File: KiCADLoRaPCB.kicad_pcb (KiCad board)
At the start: 2 copper layers, 114.8 x 80 mm, 13 parts, among them J1 Raspberry_Pi_2_3, J2 RHF-GW, J3 Jack-DC

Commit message: edge cut layer of the square case cut are refined mistakes
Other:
- board size 114.8 x 80 mm -> 114.8 x 85.1 mm
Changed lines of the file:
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@@
     (links 33)
     (no_connects 33)
-    (area 60.884999 48.184999 175.843001 128.345001)
+    (area 60.884999 47.925 175.843001 142.600001)
     (thickness 1.6)
-    (drawings 2924)
+    (drawings 2933)
     (tracks 0)
     (zones 0)
@@
     (pad 1 np_thru_hole circle (at 0 0) (size 4.3 4.3) (drill 4.3) (layers *.Cu *.Mask))
   )
-  (gr_line (start 175.768 128.27) (end 151.13 128.27) (angle 90) (layer Edge.Cuts) (width 0.15))
+  (gr_line (start 60.96 48.26) (end 60.96 55.88) (angle 90) (layer Edge.Cuts) (width 0.15))
+  (gr_line (start 60.96 58.42) (end 60.96 60.96) (angle 90) (layer Edge.Cuts) (width 0.15))
+  (gr_line (start 60.96 115.57) (end 60.96 118.11) (angle 90) (layer Edge.Cuts) (width 0.15))
+  (gr_line (start 60.96 128.27) (end 60.96 120.65) (angle 90) (layer Edge.Cuts) (width 0.15))
+  (gr_line (start 175.768 45.72) (end 175.768 48.26) (angle 90) (layer Edge.Cuts) (width 0.15))
+  (gr_line (start 60.96 45.72) (end 175.768 45.72) (angle 90) (layer Edge.Cuts) (width 0.15))
+  (gr_line (start 60.96 48.26) (end 60.96 45.72) (angle 90) (layer Edge.Cuts) (width 0.15))
+  (gr_line (start 60.96 130.81) (end 60.96 128.27) (angle 90) (layer Edge.Cuts) (width 0.15))
+  (gr_line (start 175.768 130.81) (end 175.768 128.27) (angle 90) (layer Edge.Cuts) (width 0.15))
+  (gr_line (start 60.96 130.81) (end 175.768 130.81) (angle 90) (layer Edge.Cuts) (width 0.15))
+  (gr_line (start 65.024 58.42) (end 64.77 58.42) (angle 90) (layer Edge.Cuts) (width 0.15))
+  (gr_line (start 65.024 55.88) (end 65.024 58.42) (angle 90) (layer Edge.Cuts) (width 0.15))
+  (gr_line (start 64.77 55.88) (end 65.024 55.88) (angle 90) (layer Edge.Cuts) (width 0.15))
+  (gr_line (start 65.024 120.65) (end 64.77 120.65) (angle 90) (layer Edge.Cuts) (width 0.15))
+  (gr_line (start 65.024 118.11) (end 65.024 120.65) (angle 90) (layer Edge.Cuts) (width 0.15))
+  (gr_line (start 64.77 118.11) (end 65.024 118.11) (angle 90) (layer Edge.Cuts) (width 0.15))
+  (gr_line (start 60.96 115.57) (end 60.96 114.3) (angle 90) (layer Edge.Cuts) (width 0.15))
+  (gr_line (start 64.77 118.11) (end 60.96 118.11) (angle 90) (layer Edge.Cuts) (width 0.15))
+  (gr_line (start 60.96 120.65) (end 64.77 120.65) (angle 90) (layer Edge.Cuts) (width 0.15))
   (gr_line (start 175.768 48.26) (end 175.768 128.27) (angle 90) (layer Edge.Cuts) (width 0.15))
-  (gr_line (start 151.13 48.26) (end 175.768 48.26) (angle 90) (layer Edge.Cuts) (width 0.15))
   (gr_line (start 169 59.5) (end 169 142.5) (angle 90) (layer Dwgs.User) (width 0.2))
   (gr_line (start 169 142.5) (end 169.5 142.5) (angle 90) (layer Dwgs.User) (width 0.2))
@@
   (gr_line (start 72.39 59.69) (end 115.316 59.69) (angle 90) (layer Dwgs.User) (width 0.2))
   (gr_line (start 67.818 59.69) (end 72.39 59.69) (angle 90) (layer Dwgs.User) (width 0.2))
-  (gr_line (start 67.818 59.69) (end 64.77 59.69) (angle 90) (layer Eco1.User) (width 0.2))
-  (gr_line (start 60.96 118.11) (end 60.96 128.27) (angle 90) (layer Edge.Cuts) (width 0.15))
+  (gr_line (start 67.818 57.15) (end 64.77 57.15) (angle 90) (layer Eco1.User) (width 0.2))
   (gr_line (start 60.96 60.96) (end 60.96 114.3) (angle 90) (layer Edge.Cuts) (width 0.15))
-  (gr_line (start 64.77 114.3) (end 60.96 114.3) (angle 90) (layer Edge.Cuts) (width 0.15))
-  (gr_line (start 64.77 118.11) (end 64.77 114.3) (angle 90) (layer Edge.Cuts) (width 0.15))
-  (gr_line (start 60.96 118.11) (end 64.77 118.11) (angle 90) (layer Edge.Cuts) (width 0.15))
-  (gr_line (start 60.96 48.26) (end 60.96 58.42) (angle 90) (layer Edge.Cuts) (width 0.15))
-  (gr_line (start 64.77 60.96) (end 60.96 60.96) (angle 90) (layer Edge.Cuts) (width 0.15))
-  (gr_line (start 64.77 58.42) (end 64.77 60.96) (angle 90) (layer Edge.Cuts) (width 0.15))
-  (gr_line (start 60.96 58.42) (end 64.77 58.42) (angle 90) (layer Edge.Cuts) (width 0.15))
-  (gr_line (start 151.13 48.26) (end 60.96 48.26) (angle 90) (layer Edge.Cuts) (width 0.15))
-  (gr_line (start 60.96 128.27) (end 151.13 128.27) (angle 90) (layer Edge.Cuts) (width 0.15))
+  (gr_line (start 64.77 58.42) (end 60.96 58.42) (angle 90) (layer Edge.Cuts) (width 0.15))
+  (gr_line (start 60.96 55.88) (end 64.77 55.88) (angle 90) (layer Edge.Cuts) (width 0.15))
 )

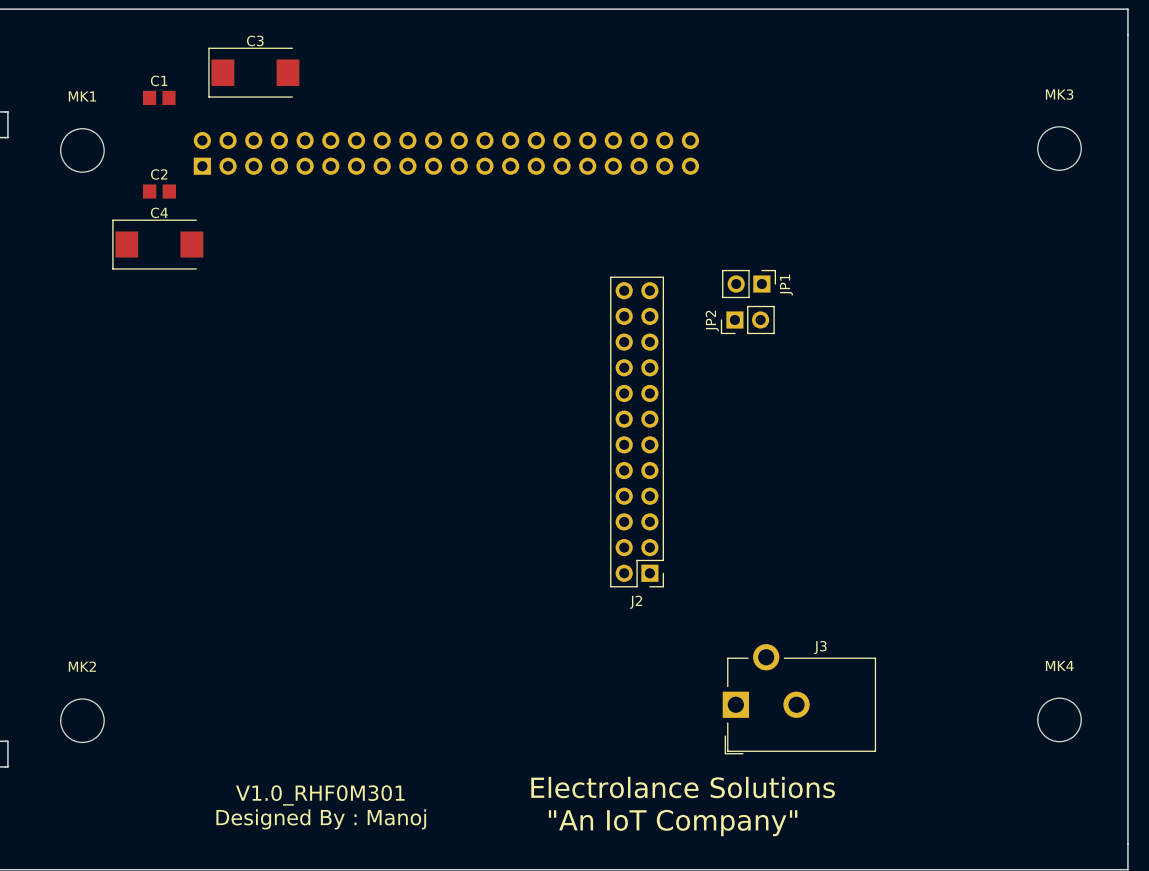
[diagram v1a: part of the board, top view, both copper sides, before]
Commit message: All holes ext PCB alignedwith case hole
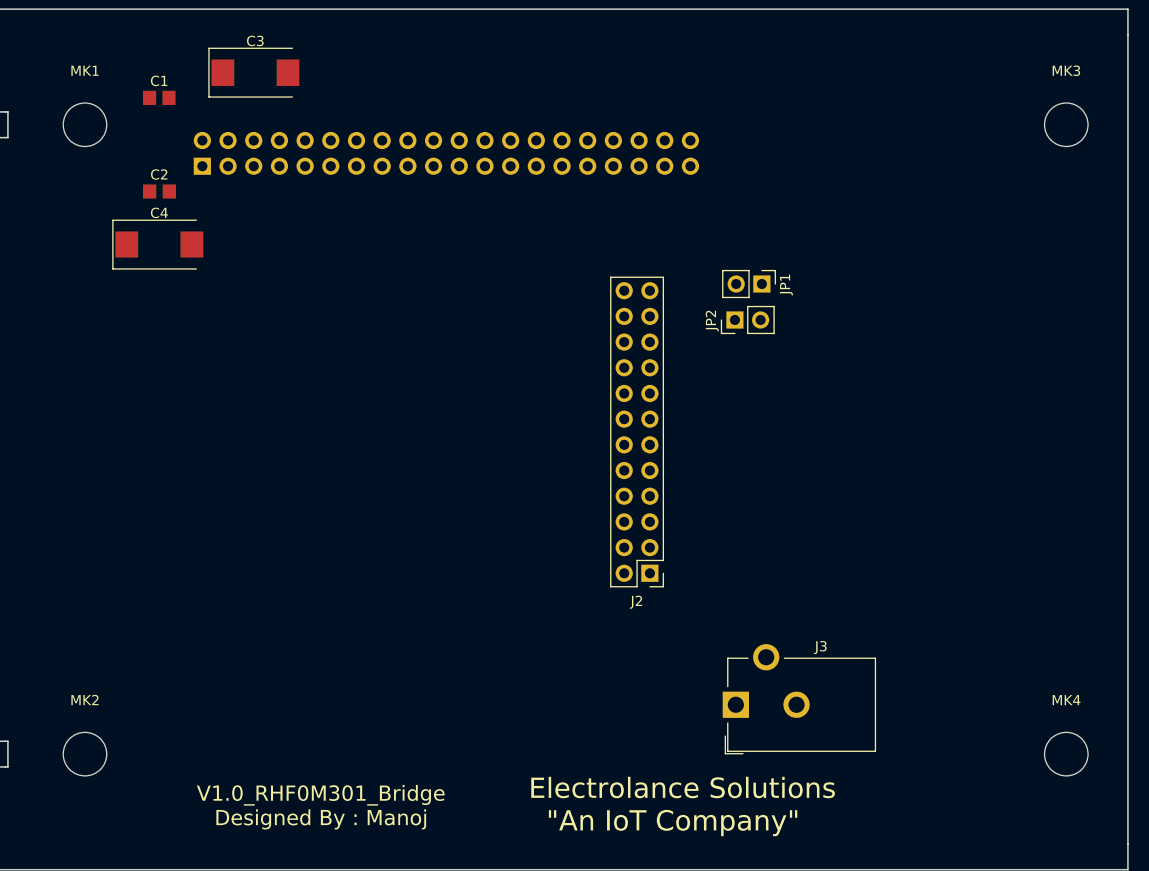
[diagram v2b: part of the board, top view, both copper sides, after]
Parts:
- moved MK4 3.45 mm to (169.7, 119.4)
- moved MK2 3.31 mm to (72.6, 119.4)
- moved MK1 2.55 mm to (72.6, 57.1)
- moved MK3 2.44 mm to (169.7, 57.1)
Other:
- board text added: "8.5 x 11.5 [cm]"
- board text added: "Edge cut till border S. Hole"
- board text added: "V1.0_RHF0M301_Bridge Designed By : Manoj"
- board text removed: "V1.0_RHF0M301 Designed By : Manoj"
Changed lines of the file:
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@@
     (links 33)
     (no_connects 33)
-    (area 60.884999 47.925 175.843001 142.600001)
+    (area 60.884999 45.644999 175.843001 130.885001)
     (thickness 1.6)
-    (drawings 2933)
+    (drawings 2956)
     (tracks 0)
     (zones 0)
@@
     (visible_elements FFFFF77F)
     (pcbplotparams
-      (layerselection 0x00030_80000001)
+      (layerselection 0x01000_00000000)
       (usegerberextensions false)
       (excludeedgelayer true)
@@
       (padsonsilk false)
       (subtractmaskfromsilk false)
-      (outputformat 1)
+      (outputformat 4)
       (mirror false)
-      (drillshape 1)
+      (drillshape 0)
       (scaleselection 1)
-      (outputdirectory ""))
+      (outputdirectory Gerber&Schematics/))
   )
   (net 0 "")
@@
   )
   (module MountingHole:MountingHole_4.3mm_M4 (layer F.Cu)
-    (at 72.39 59.69)
+    (at 72.644 57.15)
     (descr "Mounting Hole 4.3mm, no annular, M4")
     (tags "mounting hole 4.3mm no annular m4")
@@
   )
   (module MountingHole:MountingHole_4.3mm_M4 (layer F.Cu)
-    (at 72.39 116.078)
+    (at 72.644 119.38)
     (descr "Mounting Hole 4.3mm, no annular, M4")
     (tags "mounting hole 4.3mm no annular m4")
@@
   )
   (module MountingHole:MountingHole_4.3mm_M4 (layer F.Cu)
-    (at 169 59.5)
+    (at 169.672 57.15)
     (descr "Mounting Hole 4.3mm, no annular, M4")
     (tags "mounting hole 4.3mm no annular m4")
@@
   )
   (module MountingHole:MountingHole_4.3mm_M4 (layer F.Cu)
-    (at 169 116)
+    (at 169.672 119.38)
     (descr "Mounting Hole 4.3mm, no annular, M4")
     (tags "mounting hole 4.3mm no annular m4")
@@
     (pad 1 np_thru_hole circle (at 0 0) (size 4.3 4.3) (drill 4.3) (layers *.Cu *.Mask))
   )
+  (gr_line (start 67.564 119.38) (end 67.818 119.38) (angle 90) (layer Eco2.User) (width 0.2))
+  (gr_line (start 67.056 119.38) (end 67.31 119.38) (angle 90) (layer Eco2.User) (width 0.2))
+  (gr_line (start 66.548 119.38) (end 66.802 119.38) (angle 90) (layer Eco2.User) (width 0.2))
+  (gr_line (start 66.04 119.38) (end 66.294 119.38) (angle 90) (layer Eco2.User) (width 0.2))
+  (gr_line (start 65.532 119.38) (end 65.786 119.38) (angle 90) (layer Eco2.User) (width 0.2))
+  (gr_line (start 65.024 119.38) (end 65.278 119.38) (angle 90) (layer Eco2.User) (width 0.2))
+  (dimension 7.62 (width 0.3) (layer Margin)
+    (gr_text "7.620 mm" (at 69.596 37.084) (layer Margin)
+      (effects (font (size 1.5 1.5) (thickness 0.3)))
+    )
+    (feature1 (pts (xy 72.644 57.15) (xy 72.644 37.686)))
+    (feature2 (pts (xy 65.024 57.15) (xy 65.024 37.686)))
+    (crossbar (pts (xy 65.024 40.386) (xy 72.644 40.386)))
+    (arrow1a (pts (xy 72.644 40.386) (xy 71.517496 40.972421)))
+    (arrow1b (pts (xy 72.644 40.386) (xy 71.517496 39.799579)))
+    (arrow2a (pts (xy 65.024 40.386) (xy 66.150504 40.972421)))
+    (arrow2b (pts (xy 65.024 40.386) (xy 66.150504 39.799579)))
+  )
+  (dimension 4.064 (width 0.1) (layer Margin)
+    (gr_text "4.064 mm" (at 63.246 138.43) (layer Margin)
+      (effects (font (size 1 1) (thickness 0.1)))
+    )
+    (feature1 (pts (xy 65.024 120.65) (xy 65.024 137.32)))
+    (feature2 (pts (xy 60.96 120.65) (xy 60.96 137.32)))
+    (crossbar (pts (xy 60.96 134.62) (xy 65.024 134.62)))
+    (arrow1a (pts (xy 65.024 134.62) (xy 63.897496 135.206421)))
+    (arrow1b (pts (xy 65.024 134.62) (xy 63.897496 134.033579)))
+    (arrow2a (pts (xy 60.96 134.62) (xy 62.086504 135.206421)))
+    (arrow2b (pts (xy 60.96 134.62) (xy 62.086504 134.033579)))
+  )
+  (gr_text "Edge cut\ntill border\nS. Hole\n" (at 67.056 44.45) (layer Margin)
+    (effects (font (size 0.5 0.5) (thickness 0.1)))
+  )
+  (gr_line (start 79.756 57.15) (end 80.264 57.15) (angle 90) (layer Eco2.User) (width 0.2))
+  (gr_line (start 78.74 57.15) (end 79.248 57.15) (angle 90) (layer Eco2.User) (width 0.2))
+  (gr_line (start 77.724 57.15) (end 78.232 57.15) (angle 90) (layer Eco2.User) (width 0.2))
+  (gr_line (start 76.708 57.15) (end 77.216 57.15) (angle 90) (layer Eco2.User) (width 0.2))
+  (gr_line (start 75.946 57.15) (end 76.454 57.15) (angle 90) (layer Eco2.User) (width 0.2))
+  (gr_line (start 74.93 57.15) (end 75.438 57.15) (angle 90) (layer Eco2.User) (width 0.2))
+  (gr_line (start 69.342 57.15) (end 69.85 57.15) (angle 90) (layer Eco2.User) (width 0.2))
+  (gr_line (start 68.326 57.15) (end 68.834 57.15) (angle 90) (layer Eco2.User) (width 0.2))
+  (gr_line (start 67.31 57.15) (end 67.818 57.15) (angle 90) (layer Eco2.User) (width 0.2))
+  (gr_line (start 66.294 57.15) (end 66.802 57.15) (angle 90) (layer Eco2.User) (width 0.2))
+  (gr_line (start 65.024 57.15) (end 65.786 57.15) (angle 90) (layer Eco2.User) (width 0.2))
+  (dimension 3.048 (width 0.15) (layer Margin)
+    (gr_text "3.048 mm" (at 68.326 46.736) (layer Margin)
+      (effects (font (size 0.8 0.8) (thickness 0.15)))
+    )
+    (feature1 (pts (xy 68.072 57.15) (xy 68.072 47.338)))
+    (feature2 (pts (xy 65.024 57.15) (xy 65.024 47.338)))
+    (crossbar (pts (xy 65.024 50.038) (xy 68.072 50.038)))
+    (arrow1a (pts (xy 68.072 50.038) (xy 66.945496 50.624421)))
+    (arrow1b (pts (xy 68.072 50.038) (xy 66.945496 49.451579)))
+    (arrow2a (pts (xy 65.024 50.038) (xy 66.150504 50.624421)))
+    (arrow2b (pts (xy 65.024 50.038) (xy 66.150504 49.451579)))
+  )
+  (dimension 114.808 (width 0.3) (layer Margin)
+    (gr_text "114.808 mm" (at 118.364 33.956) (layer Margin)
+      (effects (font (size 1.5 1.5) (thickness 0.3)))
+    )
+    (feature1 (pts (xy 175.768 45.72) (xy 175.768 32.606)))
+    (feature2 (pts (xy 60.96 45.72) (xy 60.96 32.606)))
+    (crossbar (pts (xy 60.96 35.306) (xy 175.768 35.306)))
+    (arrow1a (pts (xy 175.768 35.306) (xy 174.641496 35.892421)))
+    (arrow1b (pts (xy 175.768 35.306) (xy 174.641496 34.719579)))
+    (arrow2a (pts (xy 60.96 35.306) (xy 62.086504 35.892421)))
+    (arrow2b (pts (xy 60.96 35.306) (xy 62.086504 34.719579)))
+  )
+  (dimension 59.69 (width 0.3) (layer Margin)
+    (gr_text "59.690 mm" (at 52.498 88.265 270) (layer Margin)
+      (effects (font (size 1.5 1.5) (thickness 0.3)))
+    )
+    (feature1 (pts (xy 60.96 118.11) (xy 51.148 118.11)))
+    (feature2 (pts (xy 60.96 58.42) (xy 51.148 58.42)))
+    (crossbar (pts (xy 53.848 58.42) (xy 53.848 118.11)))
+    (arrow1a (pts (xy 53.848 118.11) (xy 53.261579 116.983496)))
+    (arrow1b (pts (xy 53.848 118.11) (xy 54.434421 116.983496)))
+    (arrow2a (pts (xy 53.848 58.42) (xy 53.261579 59.546504)))
+    (arrow2b (pts (xy 53.848 58.42) (xy 54.434421 59.546504)))
+  )
+  (dimension 10.16 (width 0.25) (layer Margin)
+    (gr_text "10.160 mm" (at 43.942 125.73 90) (layer Margin)
+      (effects (font (size 1 1) (thickness 0.25)))
+    )
+    (feature1 (pts (xy 60.96 120.65) (xy 45.814 120.65)))
+    (feature2 (pts (xy 60.96 130.81) (xy 45.814 130.81)))
+    (crossbar (pts (xy 48.514 130.81) (xy 48.514 120.65)))
+    (arrow1a (pts (xy 48.514 120.65) (xy 49.100421 121.776504)))
+    (arrow1b (pts (xy 48.514 120.65) (xy 47.927579 121.776504)))
+    (arrow2a (pts (xy 48.514 130.81) (xy 49.100421 129.683496)))
+    (arrow2b (pts (xy 48.514 130.81) (xy 47.927579 129.683496)))
+  )
+  (dimension 10.16 (width 0.2) (layer Margin)
+    (gr_text "10.160 mm" (at 46.736 50.546 270) (layer Margin)
+      (effects (font (size 1 1) (thickness 0.2)))
+    )
+    (feature1 (pts (xy 60.96 55.88) (xy 48.1 55.88)))
+    (feature2 (pts (xy 60.96 45.72) (xy 48.1 45.72)))
+    (crossbar (pts (xy 50.8 45.72) (xy 50.8 55.88)))
+    (arrow1a (pts (xy 50.8 55.88) (xy 50.213579 54.753496)))
+    (arrow1b (pts (xy 50.8 55.88) (xy 51.386421 54.753496)))
+    (arrow2a (pts (xy 50.8 45.72) (xy 50.213579 46.846504)))
+    (arrow2b (pts (xy 50.8 45.72) (xy 51.386421 46.846504)))
+  )
+  (gr_text "8.5 x 11.5 [cm]\n" (at 249.174 155.194) (layer Margin)
+    (effects (font (size 4.5 4.5) (thickness 0.3) italic))
+  )
   (gr_line (start 60.96 48.26) (end 60.96 55.88) (angle 90) (layer Edge.Cuts) (width 0.15))
   (gr_line (start 60.96 58.42) (end 60.96 60.96) (angle 90) (layer Edge.Cuts) (width 0.15))
@@
   (gr_line (start 60.96 120.65) (end 64.77 120.65) (angle 90) (layer Edge.Cuts) (width 0.15))
   (gr_line (start 175.768 48.26) (end 175.768 128.27) (angle 90) (layer Edge.Cuts) (width 0.15))
-  (gr_line (start 169 59.5) (end 169 142.5) (angle 90) (layer Dwgs.User) (width 0.2))
   (gr_line (start 169 142.5) (end 169.5 142.5) (angle 90) (layer Dwgs.User) (width 0.2))
   (gr_line (start 115.316 59.69) (end 151.13 59.69) (angle 90) (layer Dwgs.User) (width 0.2))
@@
   (gr_line (start 137.9221 56.4664) (end 138.9481 56.6473) (layer Dwgs.User) (width 0.1))
   (gr_line (start 137.9171 56.4664) (end 137.9221 56.4664) (layer Dwgs.User) (width 0.1))
-  (gr_text "V1.0_RHF0M301\nDesigned By : Manoj\n" (at 96 124.5) (layer F.SilkS)
+  (gr_text "V1.0_RHF0M301_Bridge\nDesigned By : Manoj\n" (at 96 124.5) (layer F.SilkS)
     (effects (font (size 1.5 1.5) (thickness 0.3)))
   )
@@
   (gr_line (start 67.818 116.078) (end 133.604 116.078) (angle 90) (layer Dwgs.User) (width 0.2))
   (gr_line (start 67.818 59.69) (end 67.818 116.078) (angle 90) (layer Dwgs.User) (width 0.2))
-  (gr_line (start 64.77 116.078) (end 67.818 116.078) (angle 90) (layer Eco1.User) (width 0.2))
   (gr_line (start 72.39 59.69) (end 115.316 59.69) (angle 90) (layer Dwgs.User) (width 0.2))
   (gr_line (start 67.818 59.69) (end 72.39 59.69) (angle 90) (layer Dwgs.User) (width 0.2))
-  (gr_line (start 67.818 57.15) (end 64.77 57.15) (angle 90) (layer Eco1.User) (width 0.2))
   (gr_line (start 60.96 60.96) (end 60.96 114.3) (angle 90) (layer Edge.Cuts) (width 0.15))
   (gr_line (start 64.77 58.42) (end 60.96 58.42) (angle 90) (layer Edge.Cuts) (width 0.15))
